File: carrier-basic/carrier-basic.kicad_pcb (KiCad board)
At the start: 2 copper layers, 100 x 100 mm, 12 parts, among them J1 Conn_02x20_Counter_Clockwise, J2 Conn_02x20_Counter_Clockwise, J3 Conn_02x20_Counter_Clockwise, J4 Conn_02x20_Counter_Clockwise, J5 Conn_02x20_Counter_Clockwise, J6 Conn_02x20_Counter_Clockwise, J7 Conn_02x20_Counter_Clockwise

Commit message: Experiment with how I want to place some I/O on the basic carrier
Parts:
- removed REF**: RobotMan2412_20mm, RobotMan2412:RobotMan2412_20mm
- added J10: Conn_02x06_Odd_Even, Connector_PinSocket_2.54mm:PinSocket_2x06_P2.54mm_Horizontal, F.Cu at (162.0, 97.5)
- added J11: Conn_02x06_Odd_Even, Connector_PinSocket_2.54mm:PinSocket_2x06_P2.54mm_Horizontal, F.Cu at (162.0, 115.2)
- added J12: Conn_02x06_Odd_Even, Connector_PinSocket_2.54mm:PinSocket_2x06_P2.54mm_Horizontal, F.Cu at (162.0, 133.0)
- added J13: Conn_02x06_Odd_Even, Connector_PinSocket_2.54mm:PinSocket_2x06_P2.54mm_Horizontal, F.Cu at (162.0, 150.8)
- added J8: Conn_02x06_Odd_Even, Connector_PinSocket_2.54mm:PinSocket_2x06_P2.54mm_Horizontal, F.Cu at (162.0, 61.9)
- added J9: Conn_02x06_Odd_Even, Connector_PinSocket_2.54mm:PinSocket_2x06_P2.54mm_Horizontal, F.Cu at (162.0, 79.7)
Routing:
- net unconnected-(J10-Pin_11-Pad11): track 0.00 -> 2.04 mm
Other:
- board size 100 x 100 mm -> 150 x 150 mm

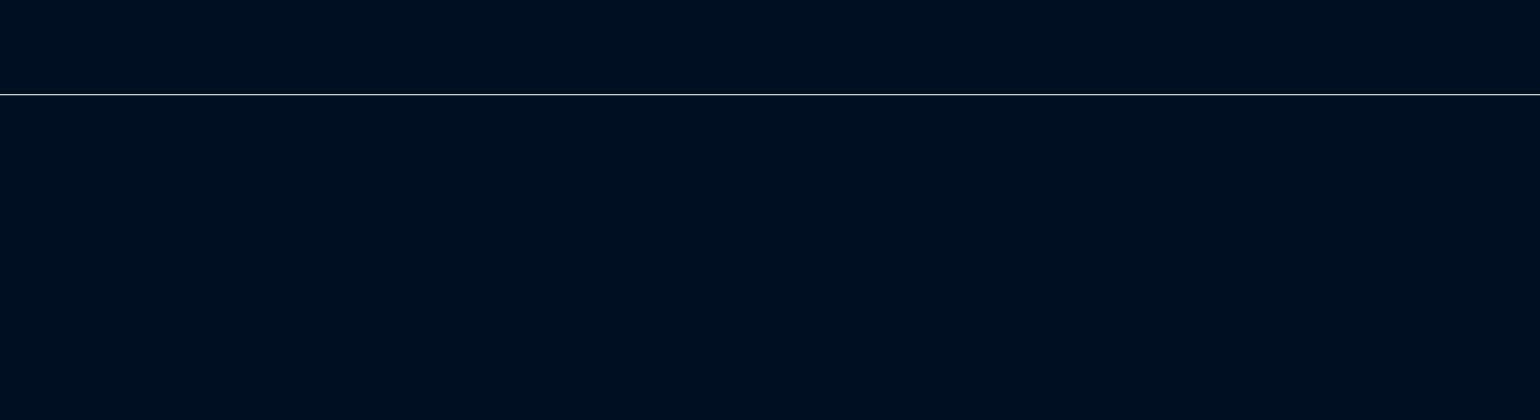
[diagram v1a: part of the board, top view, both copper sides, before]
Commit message: Make power traces on SOM thicker, more experimentallingification with carrier I/O layout
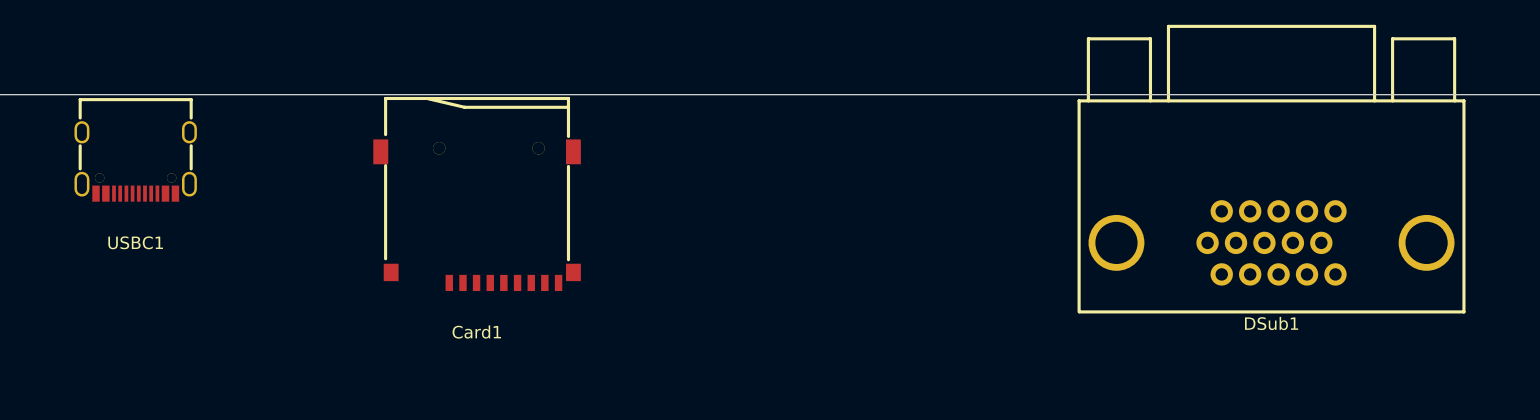
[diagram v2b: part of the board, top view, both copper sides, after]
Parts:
- added Card1: TF-01A, easyeda:TF-SMD_TF-01A, F.Cu at (72.5, 34.9)
- added DSub1: DDMRH15PFE006, easyeda:DSUB-TH_15P-P2.29-H-F_DDMRH15PFE006, F.Cu at (136.5, 36.9)
- added USBC1: TYPE-C-31-M-12, easyeda:USB-C_SMD-TYPE-C-31-M-12, F.Cu at (45.0, 30.5)
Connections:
- J1 pad 33: +3V3 -> GND
- J1 pad 35: GND -> +3V3
- J1 pad 6: GND -> +3V3
- J1 pad 8: +3V3 -> GND

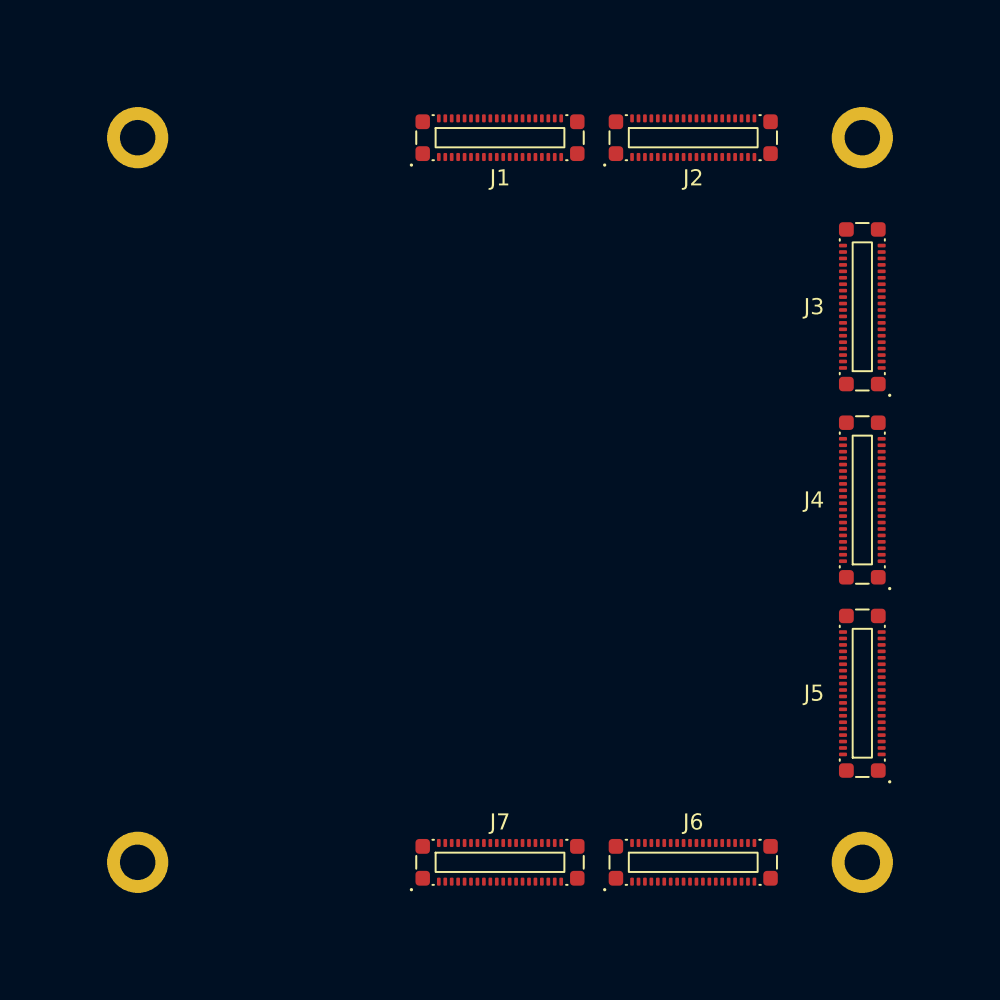
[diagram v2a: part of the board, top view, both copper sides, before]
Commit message: Fix USB-C connector symbol and footprint
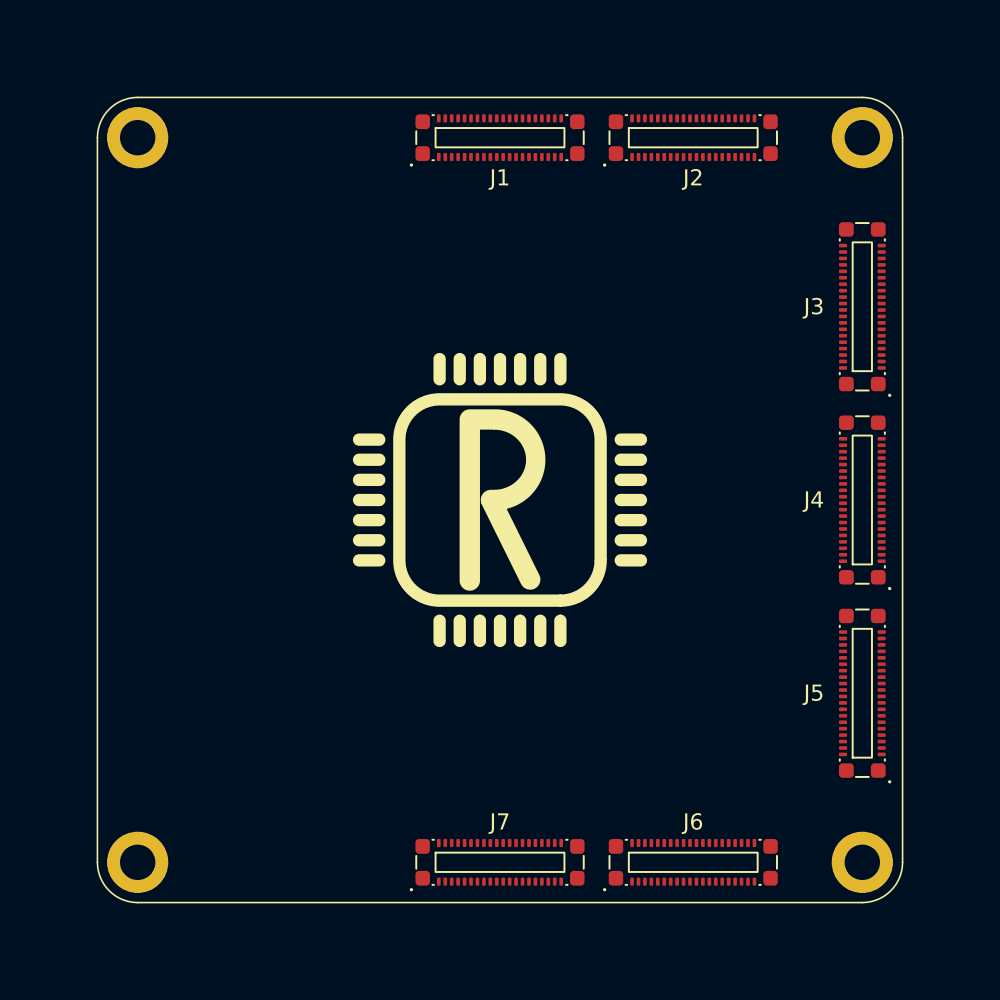
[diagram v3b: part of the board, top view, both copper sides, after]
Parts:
- added REF**: RobotMan2412_20mm, RobotMan2412:RobotMan2412_20mm, F.Cu at (100.0, 100.0)
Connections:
- USBC1 pad 0: unconnected-(USBC1-SH-Pad0) -> Net-(USBC1-SH)
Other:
- copper layers 2 -> 4
